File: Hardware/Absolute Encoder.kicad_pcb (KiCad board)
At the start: 2 copper layers, 69 x 30 mm, 21 parts, among them J1 PISO_OUT, J2 PISO_IN, U1 74LS165

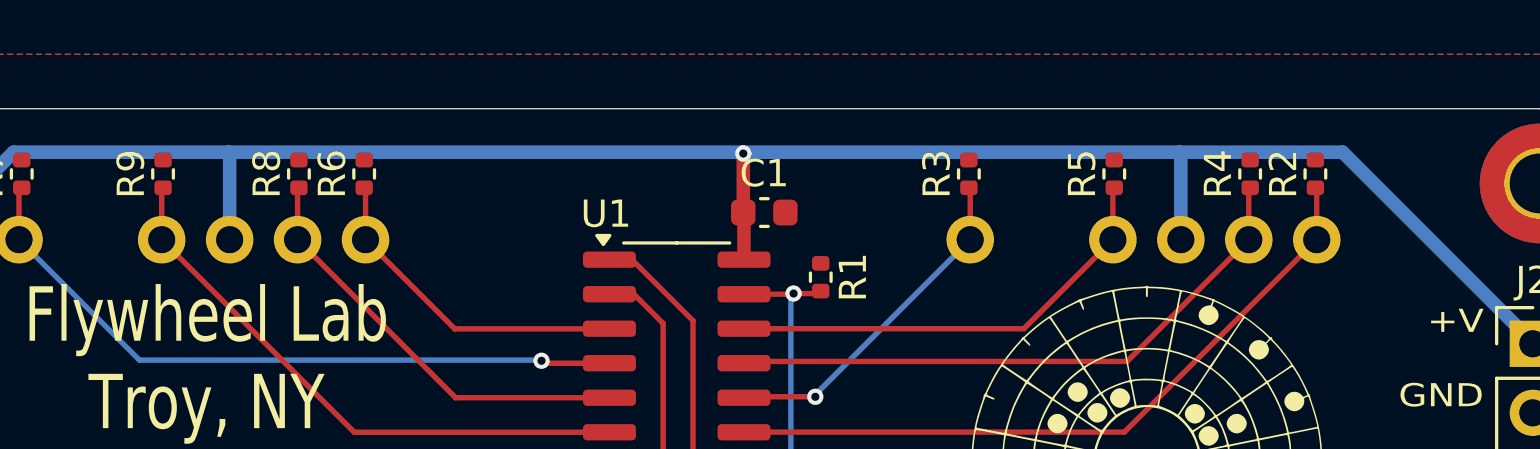
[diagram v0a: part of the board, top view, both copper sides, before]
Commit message: Update Readme
add license
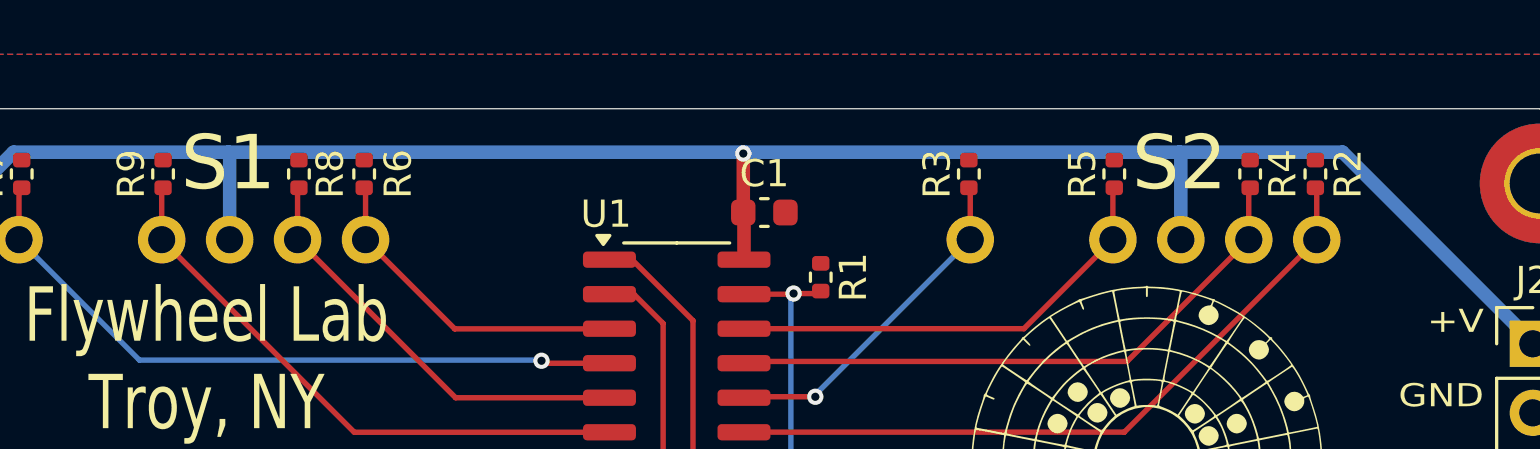
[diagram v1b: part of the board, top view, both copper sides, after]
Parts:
- added G***: LOGO, Flywheel:oshwa-logo-gear, B.Cu at (204.5, 74.5)
- renumbered S2 to S1, S1 to S2
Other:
- board text added: "S1"
- board text added: "S2"
- board text added: "hardware"
- board text added: "open"
- board text added: "source"

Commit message: updated back silk
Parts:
- moved G*** 8.30 mm to (204.5, 66.2)
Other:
- board text added: "16"
- board text added: "8"
- board text added: "ZERO POSITION"

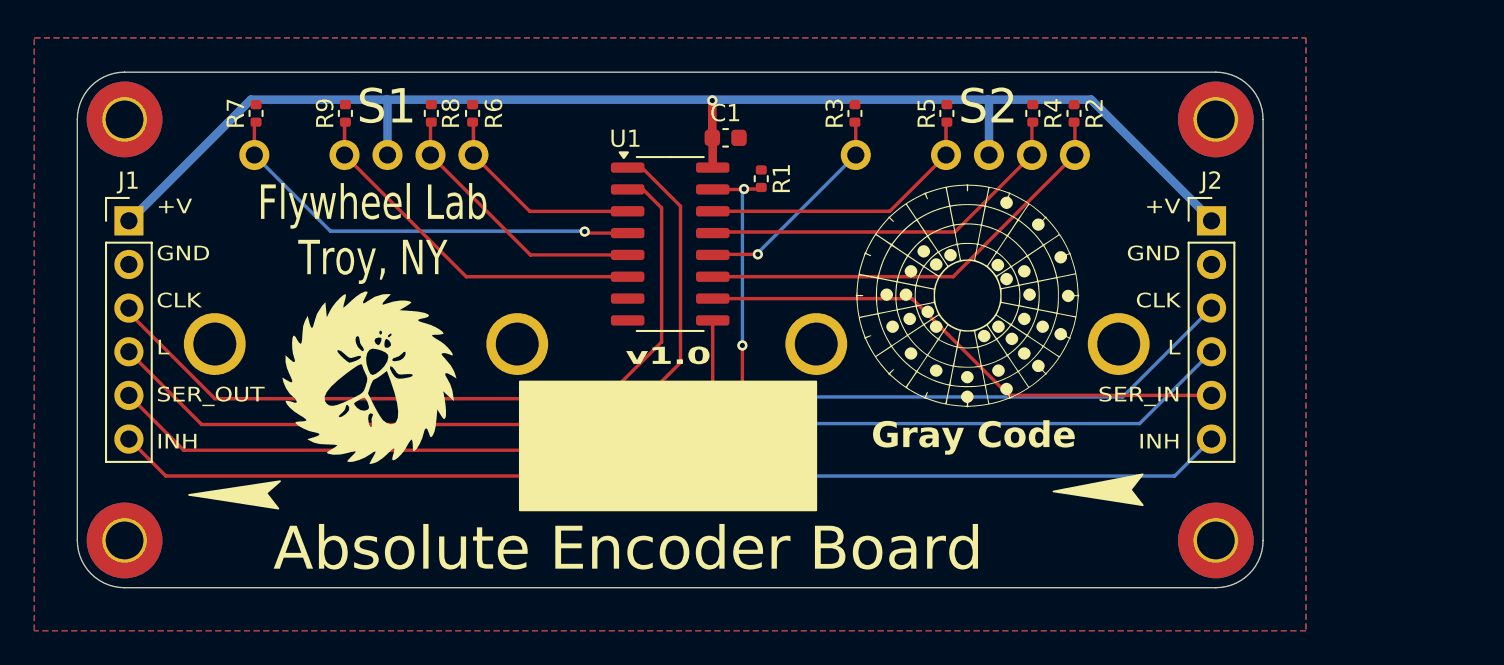
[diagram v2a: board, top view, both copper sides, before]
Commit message: Added breakaway and set encoder distance
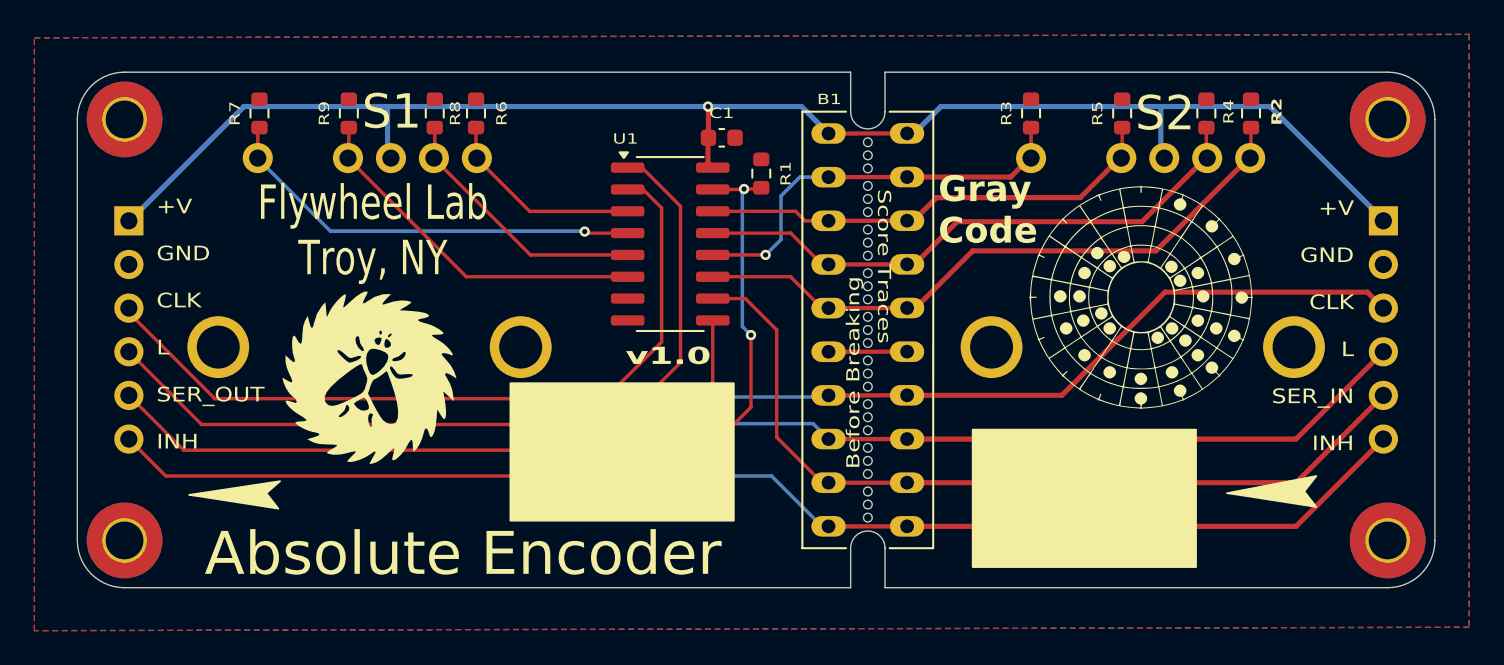
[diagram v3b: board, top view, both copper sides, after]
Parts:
- added B1: ~, AbsoluteEncoder:Breakaway_10pos, F.Cu at (213.7, 63.6)
- J1, J2: moved to B.Cu
- R1, R2, R3, R4, R5, R6, R7, R8, R9: footprint Resistor_SMD:R_0402_1005Metric -> Resistor_SMD:R_0603_1608Metric
- S1, S2: footprint Flywheel:PAC18R -> AbsoluteEncoder:PAC18R
- moved G*** 48.4 mm to (160.1, 47.0)
- moved R2 10.3 mm to (238.3, 62.4)
- moved R3 10.2 mm to (225.5, 62.4)
- moved S2 10.2 mm to (232.0, 65.0)
- moved R5 10.2 mm to (230.8, 62.4)
- moved G*** 10.1 mm to (231.9, 73.1)
- moved R4 10.1 mm to (235.7, 62.4)
- moved H1 10.0 mm to (246.2, 87.2)
- moved H2 10.0 mm to (246.2, 62.8)
- moved J2 10.0 mm to (246.0, 68.7), turned to 180 degrees
- moved R1 0.30 mm to (209.8, 65.9)
- moved S1 0.27 mm to (187.0, 65.0)
- moved C1 0.22 mm to (207.5, 63.8)
- moved R8 0.20 mm to (190.8, 62.4)
- moved R9 0.20 mm to (185.8, 62.4)
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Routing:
- net /SER_IN: track 31.4 -> 44.7 mm
- net /INH: track 85.8 -> 94.1 mm
- net /D1: track 12.7 -> 19.9 mm
- net /D2: track 22.4 -> 29.6 mm
- net /D0: track 25.9 -> 32.8 mm
- net /CLK: track 82.3 -> 88.5 mm
- net /LOAD: track 84.6 -> 90.8 mm
- net /D3: track 16.9 -> 22.7 mm
- net VDD: track 79.3 -> 84.6 mm
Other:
- board size 69 x 30 mm -> 79 x 30 mm
- board text added: "Absolute Encoder"
- board text removed: "Absolute Encoder Board"
